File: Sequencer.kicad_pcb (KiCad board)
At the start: 2 copper layers, 42.5 x 34.8 mm, 44 parts, among them J1 Screw_Terminal_01x12, J2 USB_B_Micro, SW1 Mode, U1 ATtiny814-SS, U2 TLP3123, U3 TLP3123, U4 TLP3123, U5 TLP3123, U6 MC78L05_SOT89, U7 FT230XS

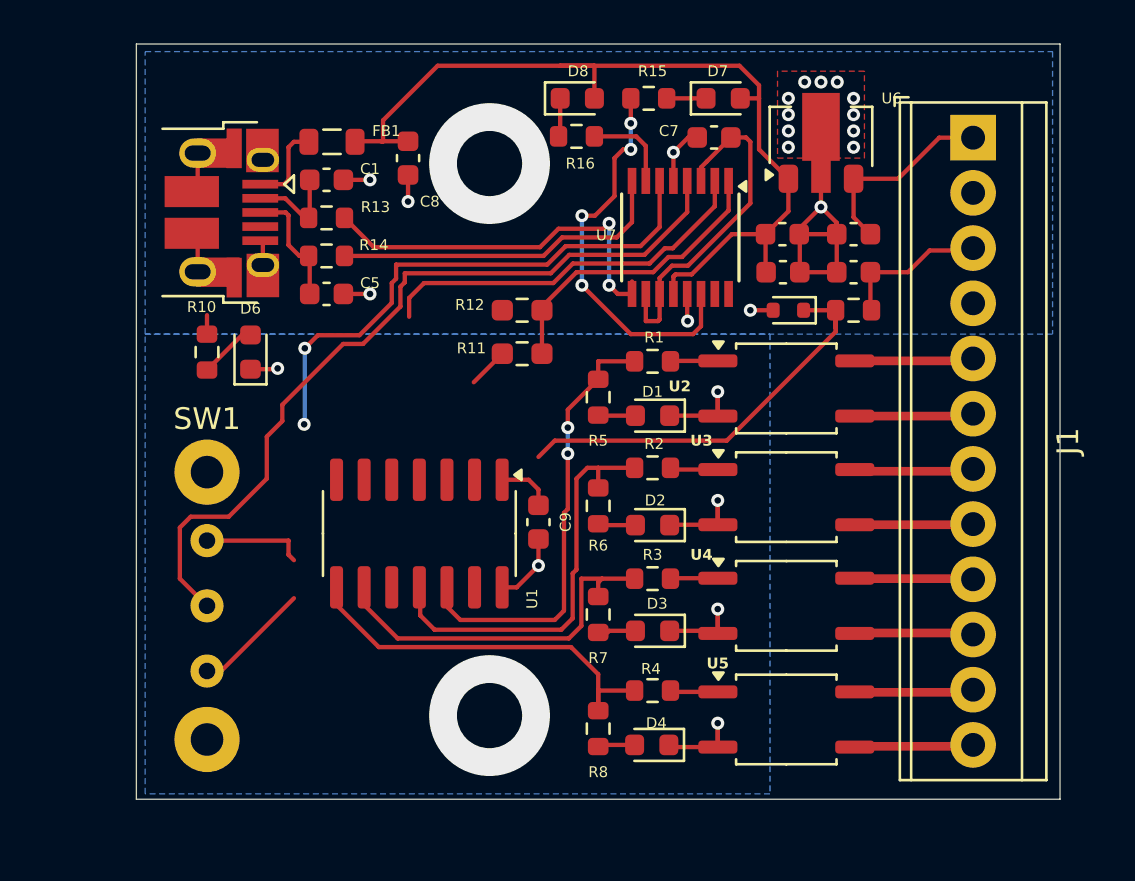
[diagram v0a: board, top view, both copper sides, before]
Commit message: Added MCU controlled LED Changed bottom fill to cover two resistors
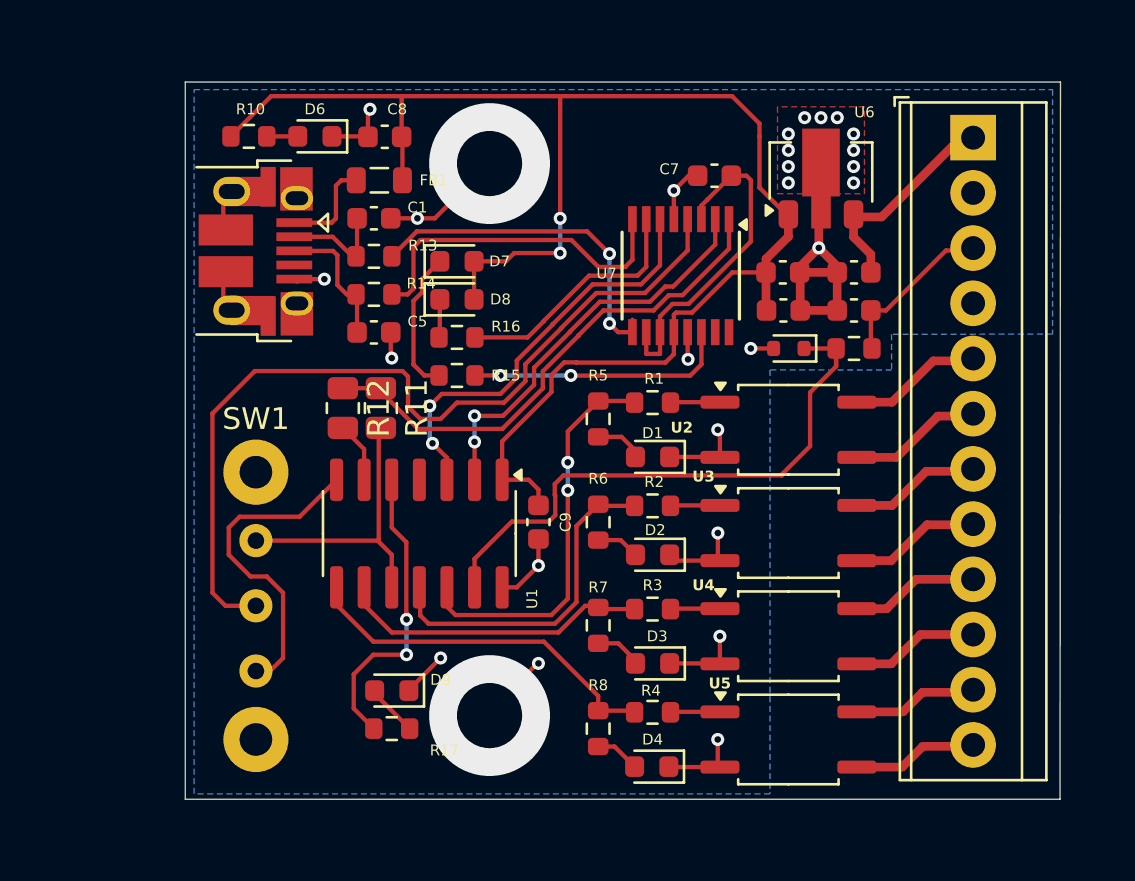
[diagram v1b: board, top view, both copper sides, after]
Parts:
- added D9: PWR, LED_SMD:LED_0603_1608Metric, F.Cu at (148.5, 77.2)
- added R17: 1K, Resistor_SMD:R_0603_1608Metric, F.Cu at (148.5, 79.0)
- D3: value IR26-21C_L110_TR8 -> SEQ3
- R11, R12: footprint Resistor_SMD:R_0603_1608Metric_Pad0.98x0.95mm_HandSolder -> Resistor_SMD:R_0805_2012Metric
- moved R15 15.5 mm to (151.5, 62.8), turned to 180 degrees
- moved D7 14.4 mm to (151.5, 57.5)
- moved D8 10.8 mm to (151.5, 59.2)
- moved R16 10.8 mm to (151.5, 61.0)
- moved D6 10.4 mm to (145.0, 51.8), turned to 180 degrees
- moved R10 10.1 mm to (141.9, 51.8), turned to 180 degrees
- moved R12 9.40 mm to (146.2, 64.2), turned to -90 degrees
- moved R11 6.96 mm to (148.0, 64.2), turned to -90 degrees
- moved C1 2.81 mm to (147.7, 55.5)
- moved C5 2.81 mm to (147.7, 60.8)
- moved FB1 2.81 mm to (147.9, 53.8)
- moved R13 2.81 mm to (147.7, 57.3)
- moved R14 2.81 mm to (147.7, 59.0)
- moved J2 2.36 mm to (142.2, 57.0)
- moved SW1 2.25 mm to (142.2, 73.3)
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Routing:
- net /5V: track 45.1 -> 73.6 mm, vias 0 -> 2
- net /LED: track 0.00 -> 14.1 mm, vias 0 -> 2
- net /SER_TXD: track 13.9 -> 23.9 mm
- net /MCU_TXD: track 5.39 -> 14.8 mm
- net GND: track 47.5 -> 55.6 mm, vias 26 -> 28
- net /KEY_MCU: track 19.9 -> 27.6 mm
- net /TXLED/: track 4.16 -> 11.4 mm
- net /UPDI: track 6.61 -> 13.3 mm
- net /RXLED/: track 18.1 -> 12.1 mm, vias 4 -> 2
- net /CTS\: track 25.2 -> 19.6 mm
- net Net-(D7-K): track 1.81 -> 6.63 mm
- net /SEQ2: track 19.2 -> 15.7 mm
- net /MCU_RXD: track 0.00 -> 2.79 mm
- net /SER_RXD: track 37.3 -> 40.0 mm
- net Net-(D9-A): track 0.00 -> 2.42 mm
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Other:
- board size 42.5 x 34.8 mm -> 40.3 x 33 mm

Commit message: Converted to USB-C connector Added zener protection to USB data wires Shuffled layout to reduce jumpers Generated BOM and gerbers for experimenting with JLCPCB
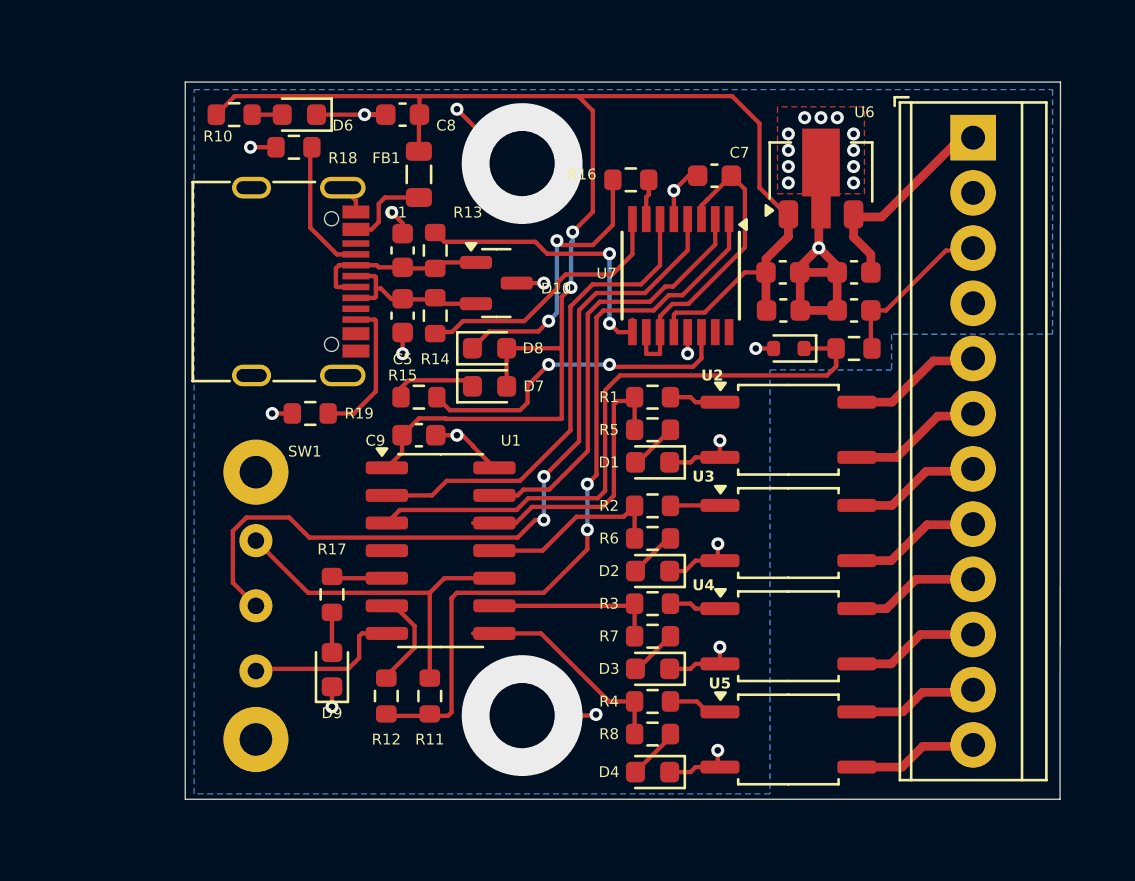
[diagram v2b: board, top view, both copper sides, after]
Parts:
- removed J2: USB_B_Micro, Connector_USB:USB_Micro-B_Amphenol_10103594-0001LF_Horizontal
- added D10: 2BZX84Cxx, Package_TO_SOT_SMD:SOT-23, F.Cu at (153.3, 58.5)
- added J3: USB_C_Receptacle_USB2.0_16P, Connector_USB:USB_C_Receptacle_G-Switch_GT-USB-7010ASV, F.Cu at (143.1, 58.4)
- added R18: 5K1, Resistor_SMD:R_0603_1608Metric, F.Cu at (144.0, 52.2)
- added R19: 5K1, Resistor_SMD:R_0603_1608Metric, F.Cu at (144.8, 64.5)
- D1, D2, D4: value IR26-21C_L110_TR8 -> Red
- D3: value SEQ3 -> Red
- D6, D9: value PWR -> Green
- D7: value RX -> Yellow
- D8: value TX -> Yellow
- R1, R2, R3, R4: value 1500 -> 1K5
- R11, R12: footprint Resistor_SMD:R_0805_2012Metric -> Resistor_SMD:R_0603_1608Metric
- R9: value 2.2K -> 2K2
- SW1: value Mode -> Switch
- moved R11 13.4 mm to (150.2, 77.5), turned to 90 degrees
- moved R12 13.4 mm to (148.2, 77.5), turned to 90 degrees
- moved R16 10.8 mm to (159.5, 53.8)
- moved C9 6.80 mm to (149.8, 65.5), turned to 0 degrees
- moved R17 6.76 mm to (145.8, 72.8), turned to -90 degrees
- moved D7 5.94 mm to (153.0, 63.2)
- moved R14 2.99 mm to (150.5, 60.0), turned to 90 degrees
- moved D9 2.91 mm to (145.8, 76.3), turned to 90 degrees
- moved R13 2.83 mm to (150.5, 57.0), turned to -90 degrees
- moved D8 2.70 mm to (153.0, 61.5)
- moved R6 2.61 mm to (160.5, 70.2), turned to 0 degrees
- moved R5 2.55 mm to (160.5, 65.2), turned to 0 degrees
- moved R7 2.55 mm to (160.5, 74.8), turned to 0 degrees
- moved R8 2.51 mm to (160.5, 79.2), turned to 0 degrees
- moved R15 2.02 mm to (149.8, 63.8)
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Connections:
- net /D+ renamed Net-(C5-Pad1)
- net /D- renamed Net-(C1-Pad1)
- net /LED renamed Net-(U1-PA7)
- U1 pad 13: /KEY_MCU -> /RTS\
- U1 pad 2: /RTS\ -> /CTS\
- U1 pad 3: /CTS\ -> /KEY_MCU
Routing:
- net Net-(U1-PA7): track 14.1 -> 2.56 mm, vias 2 -> 0
- net Net-(D8-K): track 1.77 -> 13.0 mm, vias 0 -> 2
- net /SER_TXD: track 23.9 -> 35.1 mm, vias 0 -> 2
- net /TXLED/: track 11.4 -> 1.86 mm
- net /MCU_TXD: track 14.8 -> 7.33 mm
- net /SEQ2: track 15.7 -> 8.80 mm
- net Net-(J3-CC2): track 0.00 -> 6.81 mm
- net /SEQ3: track 14.6 -> 8.04 mm
- net Net-(J3-CC1): track 0.00 -> 6.34 mm
- net /SEQ4: track 16.4 -> 10.2 mm
- net /SEQ1: track 18.3 -> 13.7 mm, vias 2 -> 0
- net /D+M: track 15.7 -> 12.2 mm
- net GND: track 55.6 -> 52.3 mm, vias 28 -> 31
- net Net-(C1-Pad1): track 5.37 -> 8.43 mm
- net /RXLED/: track 12.1 -> 15.2 mm
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
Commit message: middle of trying to remove some jumpers and make wiring more direct Trying to create room for reverse polarity protection on 12V
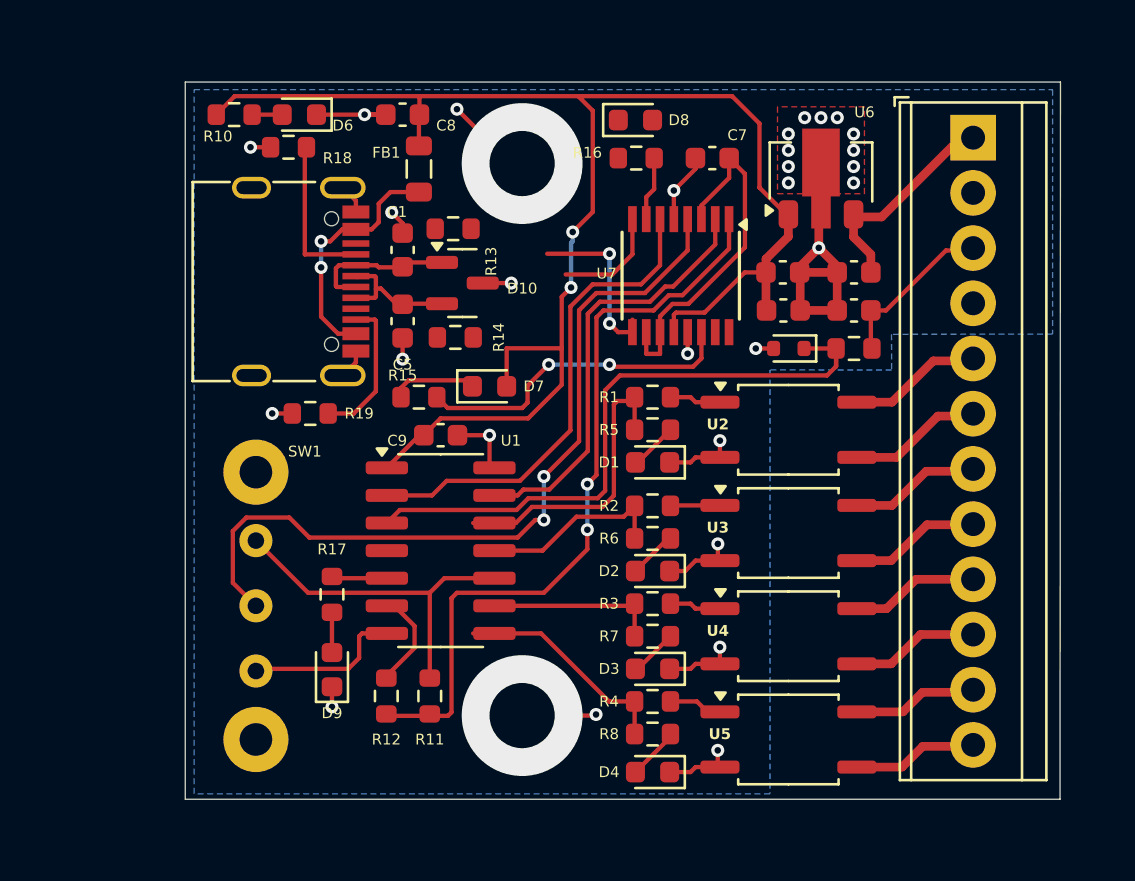
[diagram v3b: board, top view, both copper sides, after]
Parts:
- moved D8 12.5 mm to (159.7, 51.0)
- moved D10 1.56 mm to (151.8, 58.5)
- moved R14 1.36 mm to (151.4, 61.0), turned to 180 degrees
- moved R13 1.30 mm to (151.3, 56.0), turned to 180 degrees
- moved R16 1.03 mm to (159.8, 52.8)
- moved C9 1.00 mm to (150.8, 65.5)
- moved C7 0.81 mm to (163.2, 52.8)
- moved C5 0.25 mm to (149.0, 60.2)
- moved FB1 0.25 mm to (149.8, 53.2)
- moved R18 0.25 mm to (143.8, 52.2)
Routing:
- net Net-(D8-K): track 13.0 -> 0.00 mm, vias 2 -> 0
- net Net-(FB1-Pad1): track 4.01 -> 11.3 mm, vias 0 -> 2
- net /D+M: track 12.2 -> 5.07 mm
- net /D-M: track 13.3 -> 7.87 mm
- net /5V: track 73.5 -> 71.9 mm
- net /3V3: track 14.7 -> 16.3 mm
- net Net-(C1-Pad1): track 8.43 -> 6.82 mm
- net /TXLED/: track 1.86 -> 2.96 mm
- net Net-(J3-CC1): track 6.34 -> 7.31 mm
- net Net-(C5-Pad1): track 7.66 -> 6.77 mm
- net GND: track 52.3 -> 53.1 mm

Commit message: Added optocoupler on KEY line Changed to ATTinyx16 processor with 20 pins Serial select for UPDI vs Serial comms is now a pin header Added pin header for other unused signals on MCU
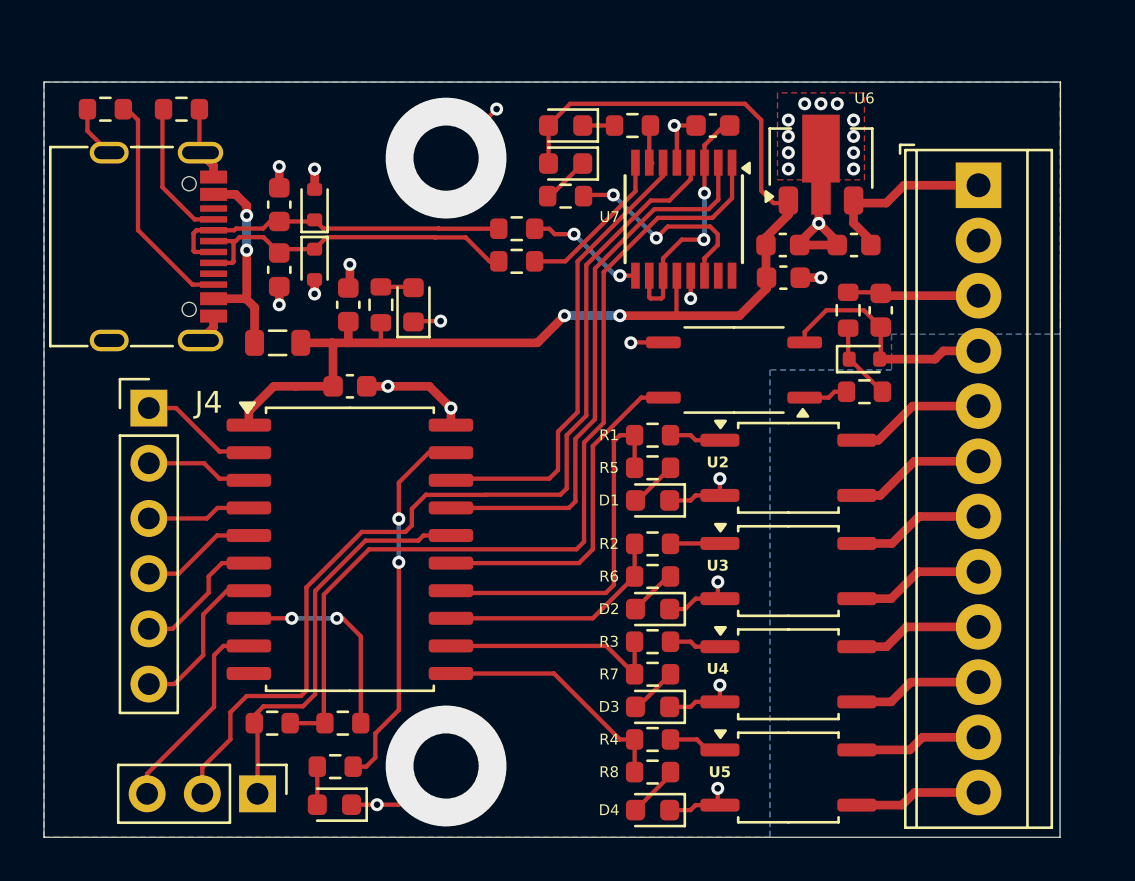
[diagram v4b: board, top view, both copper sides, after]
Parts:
- removed D10: 2BZX84Cxx, Package_TO_SOT_SMD:SOT-23
- removed SW1: Switch, Library:SLW-1277744-3a-n-d
- added D11: DZ2S036X0L, Diode_SMD:D_SOD-523, F.Cu at (144.9, 57.6)
- added D12: DZ2S036X0L, Diode_SMD:D_SOD-523, F.Cu at (144.9, 54.9)
- added J2: Serial_Mode, Connector_PinHeader_2.54mm:PinHeader_1x03_P2.54mm_Vertical, F.Cu at (142.3, 82.0)
- added J4: Extra, Connector_PinHeader_2.54mm:PinHeader_1x06_P2.54mm_Vertical, F.Cu at (137.3, 64.2)
- added R20: 1k, Resistor_SMD:R_0603_1608Metric, F.Cu at (170.2, 63.5)
- added U8: TLP185, Package_SO:SOIC-4_4.55x3.7mm_P2.54mm, F.Cu at (164.2, 62.5)
- U1: value ATtiny814-SS -> ATtiny1616-S; footprint Package_SO:SOIC-14_3.9x8.7mm_P1.27mm -> Package_SO:SOIC-20W_7.5x12.8mm_P1.27mm
- moved R19 16.9 mm to (135.3, 50.5)
- moved R15 11.5 mm to (156.5, 54.5)
- moved R10 11.1 mm to (148.0, 59.5), turned to -90 degrees
- moved D7 10.8 mm to (156.5, 53.0), turned to 180 degrees
- moved FB1 10.3 mm to (143.2, 61.2), turned to 0 degrees
- moved D6 10.2 mm to (149.5, 59.5), turned to 90 degrees
- moved C8 9.10 mm to (146.5, 59.5), turned to 90 degrees
- moved R17 7.93 mm to (145.9, 80.8), turned to 180 degrees
- moved R11 7.36 mm to (143.0, 78.8), turned to 180 degrees
- moved J3 6.74 mm to (136.6, 56.8)
- moved D9 6.21 mm to (145.9, 82.5), turned to 180 degrees
- moved C5 6.15 mm to (143.3, 57.9)
- moved C1 6.05 mm to (143.3, 54.9)
- moved R18 5.23 mm to (138.8, 50.5), turned to 180 degrees
- moved C9 4.74 mm to (146.6, 63.2)
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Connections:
- net /KEY_IN renamed /KEY+
- net /SER_TXD renamed /TXD_U
- C6 pad 2: GND -> /KEY-
- D5 pad 1: /KEY_MCU -> Net-(D5-K)
- D5 pad 2: GND -> /KEY-
- J1 pad 4: GND -> /KEY-
- R12 pad 2: /MCU_RXD -> /RXD_M
- R17 pad 1: Net-(U1-PA7) -> Net-(U1-PA3)
- R9 pad 2: /KEY_MCU -> Net-(D5-K)
- U1 pad 10: /UPDI -> unconnected-(U1-PB1-Pad10)
- U1 pad 11: /SEQ2 -> /SEQ4
- U1 pad 12: /SEQ1 -> /SEQ3
- U1 pad 13: /RTS\ -> /SEQ2
- U1 pad 14: GND -> /SEQ1
- U1 pad 2: /CTS\ -> Net-(J4-Pin_1)
- U1 pad 3: /KEY_MCU -> Net-(J4-Pin_2)
- U1 pad 4: unconnected-(U1-PA6-Pad4) -> Net-(J4-Pin_3)
- U1 pad 5: Net-(U1-PA7) -> Net-(J4-Pin_4)
- U1 pad 6: /MCU_RXD -> Net-(J4-Pin_5)
- U1 pad 7: /MCU_TXD -> Net-(J4-Pin_6)
- U1 pad 8: /SEQ4 -> /RXD_M
- U1 pad 9: /SEQ3 -> /TXD_M
- U7 pad 4: /SER_RXD -> /RXD_U
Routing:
- net /RXD_U: track 0.00 -> 45.1 mm
- net /SER_RXD: track 37.1 -> 0.00 mm, vias 2 -> 0
- net /KEY_MCU: track 29.7 -> 0.00 mm
- net /5V: track 71.9 -> 54.0 mm
- net Net-(U1-PA3): track 0.00 -> 17.4 mm, vias 0 -> 2
- net /KEY_M: track 0.00 -> 15.7 mm
- net /KEY-: track 0.00 -> 10.9 mm
- net /RXD_M: track 0.00 -> 9.49 mm, vias 0 -> 2
- net Net-(D11-K): track 6.77 -> 16.2 mm
- net /TXD_M: track 0.00 -> 9.43 mm
- net Net-(D12-K): track 6.82 -> 16.2 mm
- net Net-(J4-Pin_6): track 0.00 -> 7.48 mm
- net /MCU_TXD: track 7.33 -> 0.00 mm
- net /TXD_U: track 35.1 -> 42.2 mm, vias 2 -> 0
- net Net-(J4-Pin_5): track 0.00 -> 6.29 mm
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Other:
- board size 40.3 x 33 mm -> 46.8 x 34.8 mm
